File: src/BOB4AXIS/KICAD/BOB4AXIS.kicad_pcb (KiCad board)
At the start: 2 copper layers, 100 x 93 mm, 49 parts, among them J1 Screw_Terminal_01x03, J2 Screw_Terminal_01x03, J3 Screw_Terminal_01x03, J4 Screw_Terminal_01x03, J5 Screw_Terminal_01x08, J6 Screw_Terminal_01x08, J7 Screw_Terminal_01x08, J8 Screw_Terminal_01x08, J9 Conn_02x13_Odd_Even, U1 LTV-814, U2 LTV-814, U3 LTV-814, U4 LTV-814, U5 AM26LS31CD, U6 AM26LS31CD, U7 KF142V-5_08-2P, U8 74HC86, U9 AM26LS31CD

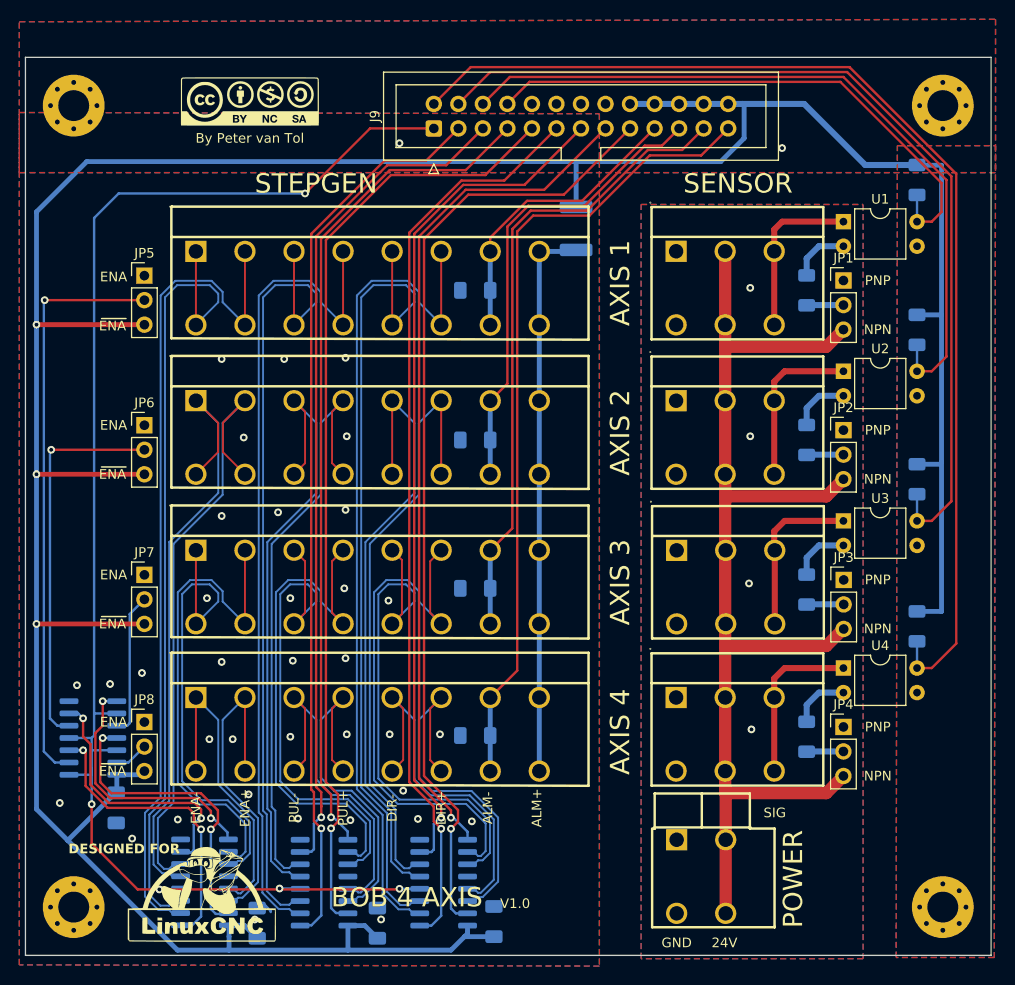
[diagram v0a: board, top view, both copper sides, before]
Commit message: Add pull-down resistor on ENA
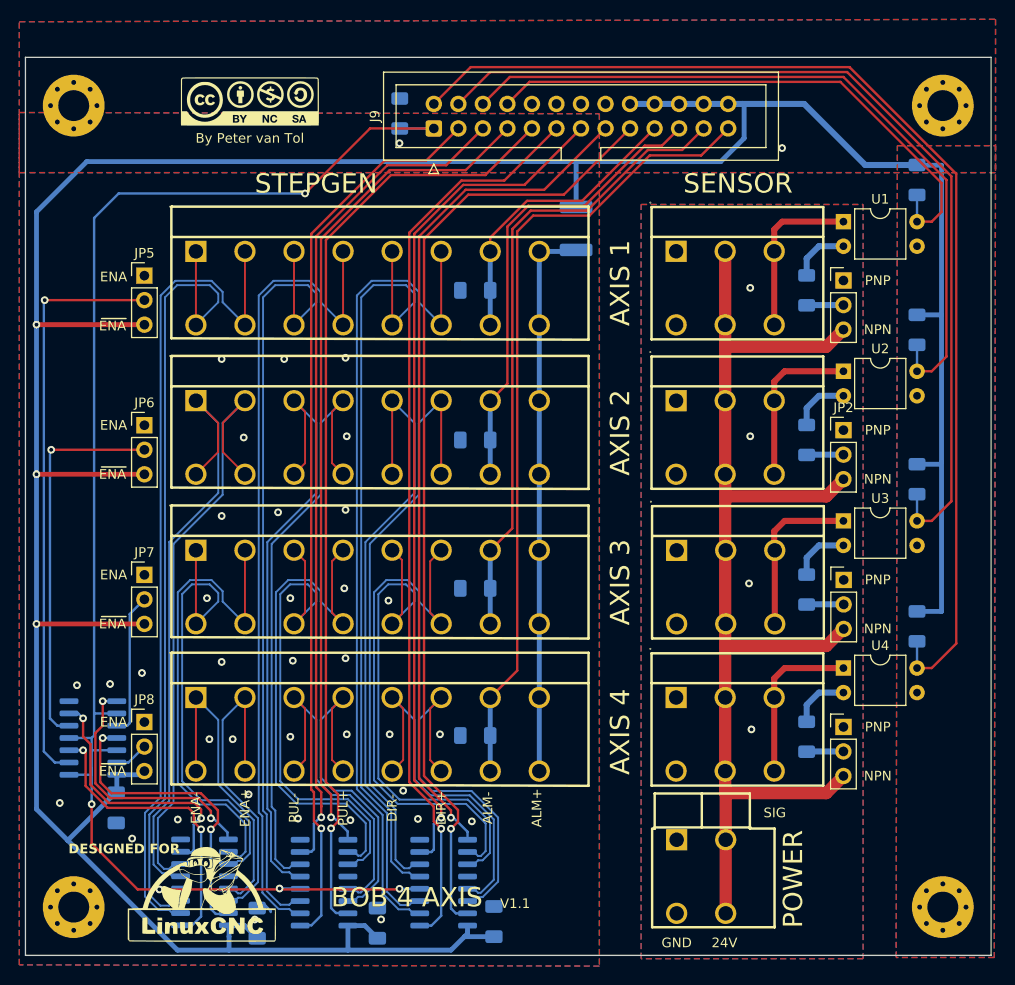
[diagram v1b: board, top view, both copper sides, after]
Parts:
- added G***: LOGO, LOGO, B.Cu at (4.83, 34.4)
- added R13: 10k, Resistor_SMD:R_1206_3216Metric_Pad1.30x1.75mm_HandSolder, B.Cu at (38.8, 5.82)
- R1, R3, R5: value R -> 1k
- R10, R11, R12, R2, R4, R6, R8, R9: value R -> 10k
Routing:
- net ENA: track 155.1 -> 158.6 mm
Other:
- board text added: "26LS31"
- board text added: "75HC86"
- board text added: "JLCJLCJLCJLC"
- board text added: "REQUIRED HUB75HAT SETTINGS: - breakout power ENABLED - pull-up / down DISABLED (remove jumper)"
- board text added: "V1.1"
- board text removed: "V1.0"
